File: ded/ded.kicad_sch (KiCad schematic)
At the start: 2 parts

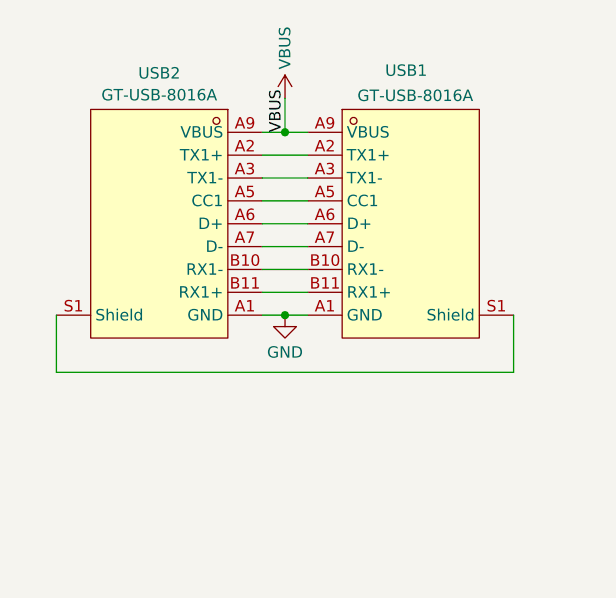
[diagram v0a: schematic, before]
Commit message: ded revision: new usb part, better trace/via routing for stability, better stiffener plan
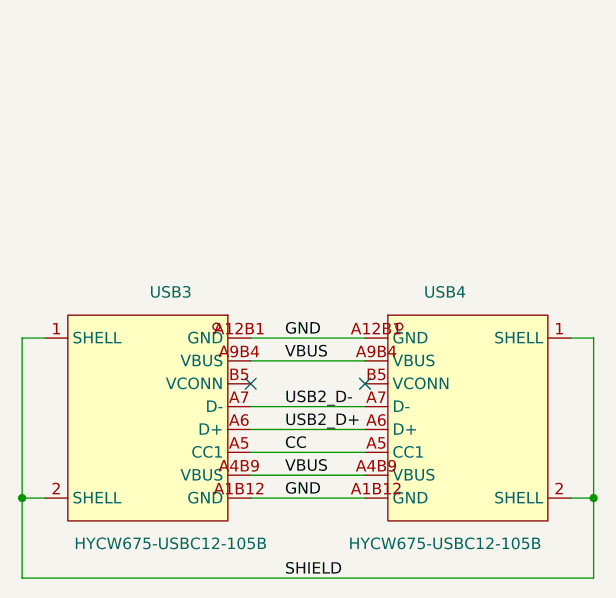
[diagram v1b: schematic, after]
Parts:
- removed USB1, USB2: GT-USB-8016A, ded:USB-TYPE-C-SMD_GT-USB-8016A, symbol ded:GT-USB-8016A
- added USB3, USB4: HYCW675-USBC12-105B, ded:USB-C-SMD_HYCW675-USBC12-105B, symbol ded:HYCW675-USBC12-105B
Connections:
- net GND: now also USB3.A12B1 (GND), USB3.A1B12 (GND), USB4.A12B1 (GND), USB4.A1B12 (GND)
- net VBUS: now also USB3.A4B9 (VBUS), USB3.A9B4 (VBUS), USB4.A4B9 (VBUS), USB4.A9B4 (VBUS)
- new net CC: USB3.A5 (CC1), USB4.A5 (CC1)
- new net SHIELD: USB3.1 (SHELL), USB3.2 (SHELL), USB4.1 (SHELL), USB4.2 (SHELL)
- new net USB2_D+: USB3.A6 (D+), USB4.A6 (D+)
- new net USB2_D-: USB3.A7 (D-), USB4.A7 (D-)
- no-connect marks 0 -> 2

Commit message: coupler usb part change
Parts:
- USB3, USB4: value HYCW675-USBC12-105B -> HYCW676-USBC12-105B; symbol ded:HYCW675-USBC12-105B -> ded:HYCW676-USBC12-105B; LCSC Part C53436585 -> C53436586; MPN HYCW675-USBC12-105B -> HYCW676-USBC12-105B
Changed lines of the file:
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@@
 	)
 	(symbol
-		(lib_id "ded:HYCW675-USBC12-105B")
+		(lib_id "ded:HYCW676-USBC12-105B")
 		(at 77.47 60.96 0)
 		(mirror y)
@@
 			)
 		)
-		(property "Value" "HYCW675-USBC12-105B"
+		(property "Value" "HYCW676-USBC12-105B"
 			(at 77.47 74.93 0)
 			(effects
@@
 			)
 		)
-		(property "Datasheet" "https://www.lcsc.com/datasheet/C53436585.pdf"
+		(property "Datasheet" "https://www.lcsc.com/datasheet/C53436586.pdf"
 			(at 77.47 60.96 0)
 			(effects
@@
 			)
 		)
-		(property "MPN" "HYCW675-USBC12-105B"
+		(property "MPN" "HYCW676-USBC12-105B"
 			(at 77.47 60.96 0)
 			(effects
@@
 			)
 		)
-		(property "LCSC Part" "C53436585"
+		(property "LCSC Part" "C53436586"
 			(at 77.47 60.96 0)
 			(effects
@@
 	)
 	(symbol
-		(lib_id "ded:HYCW675-USBC12-105B")
+		(lib_id "ded:HYCW676-USBC12-105B")
 		(at 107.95 60.96 0)
 		(unit 1)
@@
 			)
 		)
-		(property "Value" "HYCW675-USBC12-105B"
+		(property "Value" "HYCW676-USBC12-105B"
 			(at 107.95 74.93 0)
 			(effects
@@
 			)
 		)
-		(property "Datasheet" "https://www.lcsc.com/datasheet/C53436585.pdf"
+		(property "Datasheet" "https://www.lcsc.com/datasheet/C53436586.pdf"
 			(at 107.95 60.96 0)
 			(effects
@@
 			)
 		)
-		(property "MPN" "HYCW675-USBC12-105B"
+		(property "MPN" "HYCW676-USBC12-105B"
 			(at 107.95 60.96 0)
 			(effects
@@
 			)
 		)
-		(property "LCSC Part" "C53436585"
+		(property "LCSC Part" "C53436586"
 			(at 107.95 60.96 0)
 			(effects
